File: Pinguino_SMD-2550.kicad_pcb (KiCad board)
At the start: 2 copper layers, 25.4 x 25.4 mm, 17 parts, among them P1 USB_OTG, P2 CONN_01X08, P3 CONN_01X02, P4 CONN_01X10, SW1 SW Reset, Y1 20Mhz

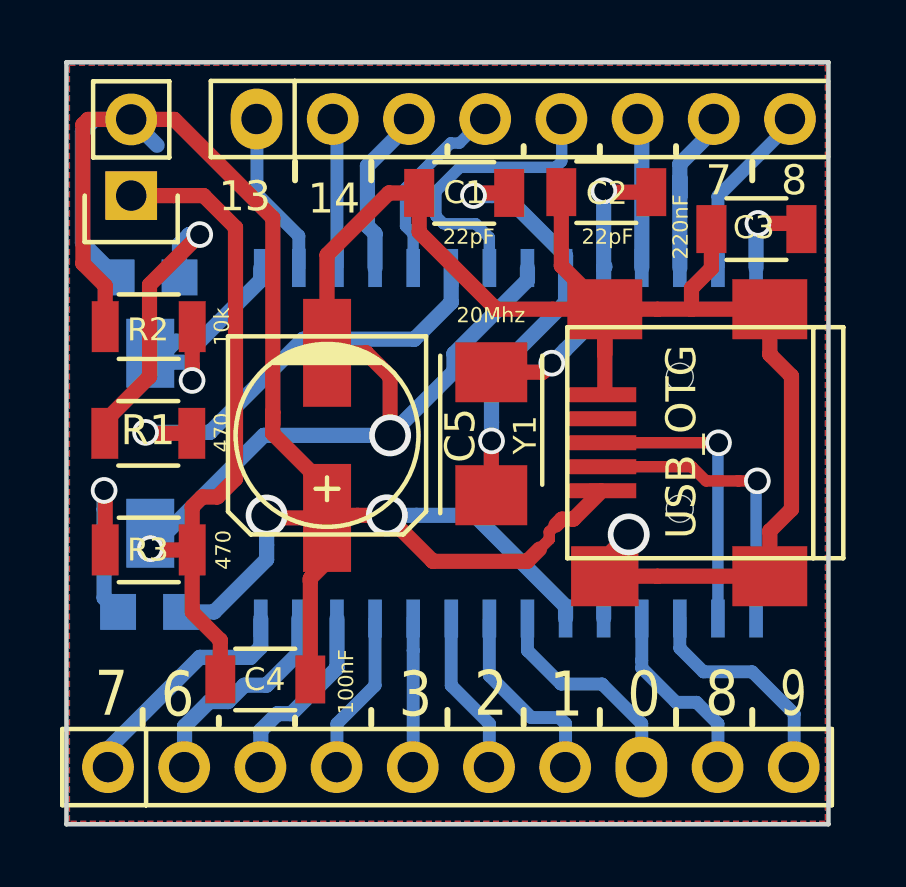
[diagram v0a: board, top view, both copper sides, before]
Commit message: Modify README.md file, updated BOM and add OSHW logo in SS layer.
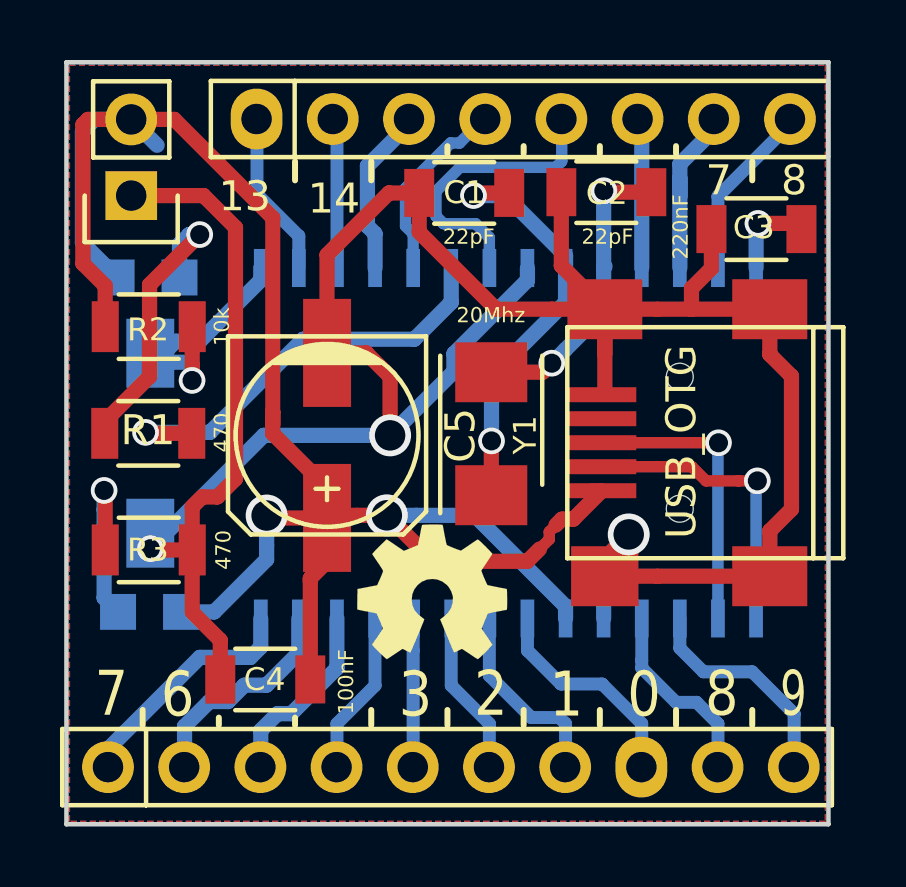
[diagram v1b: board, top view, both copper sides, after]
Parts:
- added G***: LOGO, LOGO, F.Cu at (42.7, 38.5)
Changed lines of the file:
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@@
 (kicad_pcb (version 4) (host pcbnew 4.0.2+dfsg1-2~bpo8+1-stable)
   (general
-    (links 0)
+    (links 51)
     (no_connects 0)
     (area 30.404999 20.752999 55.955001 46.303001)
@@
     (tracks 278)
     (zones 0)
-    (modules 17)
+    (modules 18)
     (nets 30)
   )
@@
   )
   (setup
-    (last_trace_width 0.508)
+    (last_trace_width 0.1524)
     (user_trace_width 0.1524)
     (user_trace_width 0.254)
@@
     (uvia_drill 0.254)
   )
+  (module LOGO (layer F.Cu)
+    (at 42.672 38.481)
+    (fp_text reference G*** (at 0 2.65176) (layer F.SilkS) hide
+      (effects (font (size 0.22606 0.22606) (thickness 0.04318)))
+    )
+    (fp_text value LOGO (at 0 -2.65176) (layer F.SilkS) hide
+      (effects (font (size 0.22606 0.22606) (thickness 0.04318)))
+    )
+    (fp_poly (pts (xy -1.51384 2.24536) (xy -1.48844 2.23012) (xy -1.43002 2.19456) (xy -1.3462 2.13868)
+      (xy -1.24714 2.07264) (xy -1.14808 2.0066) (xy -1.0668 1.95326) (xy -1.01092 1.91516)
+      (xy -0.98552 1.90246) (xy -0.97282 1.90754) (xy -0.9271 1.9304) (xy -0.85852 1.96596)
+      (xy -0.81788 1.98628) (xy -0.75692 2.01168) (xy -0.7239 2.0193) (xy -0.71882 2.00914)
+      (xy -0.69596 1.96088) (xy -0.6604 1.8796) (xy -0.61468 1.77038) (xy -0.5588 1.64338)
+      (xy -0.50292 1.50876) (xy -0.4445 1.36906) (xy -0.38862 1.23444) (xy -0.34036 1.11506)
+      (xy -0.29972 1.01854) (xy -0.27432 0.94996) (xy -0.26416 0.92202) (xy -0.2667 0.9144)
+      (xy -0.29972 0.88392) (xy -0.35306 0.84328) (xy -0.47244 0.74676) (xy -0.58928 0.60198)
+      (xy -0.6604 0.43688) (xy -0.68326 0.25146) (xy -0.66294 0.08128) (xy -0.5969 -0.08128)
+      (xy -0.4826 -0.2286) (xy -0.3429 -0.33782) (xy -0.18034 -0.4064) (xy 0 -0.42926)
+      (xy 0.17272 -0.40894) (xy 0.34036 -0.3429) (xy 0.48768 -0.23114) (xy 0.55118 -0.16002)
+      (xy 0.63754 -0.01016) (xy 0.6858 0.14732) (xy 0.69088 0.18796) (xy 0.68326 0.36322)
+      (xy 0.63246 0.5334) (xy 0.53848 0.68326) (xy 0.40894 0.80772) (xy 0.3937 0.81788)
+      (xy 0.33528 0.8636) (xy 0.29464 0.89408) (xy 0.26416 0.91948) (xy 0.48768 1.45796)
+      (xy 0.52324 1.54178) (xy 0.5842 1.6891) (xy 0.63754 1.8161) (xy 0.68072 1.9177)
+      (xy 0.7112 1.98374) (xy 0.7239 2.01168) (xy 0.7239 2.01422) (xy 0.74422 2.01676)
+      (xy 0.78486 2.00152) (xy 0.86106 1.96596) (xy 0.90932 1.94056) (xy 0.96774 1.91262)
+      (xy 0.99314 1.90246) (xy 1.016 1.91516) (xy 1.06934 1.95072) (xy 1.15062 2.00406)
+      (xy 1.24714 2.06756) (xy 1.33858 2.13106) (xy 1.4224 2.18694) (xy 1.48336 2.22504)
+      (xy 1.51384 2.24282) (xy 1.51892 2.24282) (xy 1.54432 2.22758) (xy 1.59258 2.18694)
+      (xy 1.66624 2.11836) (xy 1.77038 2.01422) (xy 1.78562 1.99898) (xy 1.87198 1.91262)
+      (xy 1.94056 1.83896) (xy 1.98628 1.78816) (xy 2.00406 1.7653) (xy 2.00406 1.7653)
+      (xy 1.98882 1.73482) (xy 1.95072 1.67386) (xy 1.89484 1.5875) (xy 1.82626 1.48844)
+      (xy 1.64846 1.22936) (xy 1.74498 0.98552) (xy 1.77546 0.90932) (xy 1.81356 0.82042)
+      (xy 1.8415 0.75438) (xy 1.85674 0.72644) (xy 1.88214 0.71628) (xy 1.95072 0.70104)
+      (xy 2.04724 0.68072) (xy 2.16154 0.6604) (xy 2.2733 0.64008) (xy 2.37236 0.61976)
+      (xy 2.44348 0.60706) (xy 2.4765 0.59944) (xy 2.48412 0.59436) (xy 2.49174 0.57912)
+      (xy 2.49428 0.5461) (xy 2.49682 0.48514) (xy 2.49936 0.39116) (xy 2.49936 0.25146)
+      (xy 2.49936 0.23622) (xy 2.49682 0.10668) (xy 2.49428 0) (xy 2.49174 -0.06604)
+      (xy 2.48666 -0.09398) (xy 2.48666 -0.09398) (xy 2.45618 -0.1016) (xy 2.38506 -0.11684)
+      (xy 2.286 -0.13462) (xy 2.16662 -0.15748) (xy 2.159 -0.16002) (xy 2.04216 -0.18288)
+      (xy 1.9431 -0.2032) (xy 1.87198 -0.21844) (xy 1.84404 -0.2286) (xy 1.83642 -0.23622)
+      (xy 1.81356 -0.28194) (xy 1.78054 -0.3556) (xy 1.7399 -0.4445) (xy 1.7018 -0.53848)
+      (xy 1.66878 -0.6223) (xy 1.64592 -0.68326) (xy 1.6383 -0.7112) (xy 1.64084 -0.71374)
+      (xy 1.65862 -0.74168) (xy 1.69926 -0.80264) (xy 1.75514 -0.88646) (xy 1.82372 -0.98806)
+      (xy 1.8288 -0.99568) (xy 1.89738 -1.09474) (xy 1.95326 -1.1811) (xy 1.98882 -1.23952)
+      (xy 2.00406 -1.26746) (xy 2.00406 -1.27) (xy 1.9812 -1.30048) (xy 1.9304 -1.35636)
+      (xy 1.85674 -1.43256) (xy 1.77038 -1.52146) (xy 1.74244 -1.54686) (xy 1.64338 -1.64338)
+      (xy 1.57734 -1.70434) (xy 1.53416 -1.73736) (xy 1.51384 -1.74498) (xy 1.51384 -1.74498)
+      (xy 1.48336 -1.7272) (xy 1.41986 -1.68656) (xy 1.33604 -1.62814) (xy 1.23444 -1.55956)
+      (xy 1.22682 -1.55448) (xy 1.12776 -1.4859) (xy 1.04394 -1.43002) (xy 0.98552 -1.38938)
+      (xy 0.95758 -1.37414) (xy 0.95504 -1.37414) (xy 0.9144 -1.38684) (xy 0.84328 -1.41224)
+      (xy 0.75438 -1.44526) (xy 0.66294 -1.48336) (xy 0.57912 -1.51892) (xy 0.51562 -1.54686)
+      (xy 0.48514 -1.56464) (xy 0.48514 -1.56464) (xy 0.47498 -1.6002) (xy 0.4572 -1.6764)
+      (xy 0.43688 -1.778) (xy 0.41148 -1.89992) (xy 0.40894 -1.92024) (xy 0.38608 -2.03962)
+      (xy 0.3683 -2.13868) (xy 0.35306 -2.20726) (xy 0.34544 -2.2352) (xy 0.3302 -2.23774)
+      (xy 0.27178 -2.24282) (xy 0.18288 -2.24536) (xy 0.07366 -2.24536) (xy -0.0381 -2.24536)
+      (xy -0.14732 -2.24282) (xy -0.2413 -2.24028) (xy -0.30988 -2.2352) (xy -0.33782 -2.23012)
+      (xy -0.33782 -2.22758) (xy -0.34798 -2.18948) (xy -0.36576 -2.11582) (xy -0.38608 -2.01168)
+      (xy -0.40894 -1.88976) (xy -0.41402 -1.8669) (xy -0.43688 -1.75006) (xy -0.4572 -1.651)
+      (xy -0.4699 -1.58496) (xy -0.47752 -1.55702) (xy -0.49022 -1.55194) (xy -0.53848 -1.53162)
+      (xy -0.61722 -1.4986) (xy -0.71628 -1.45796) (xy -0.94488 -1.36652) (xy -1.22682 -1.55702)
+      (xy -1.25222 -1.5748) (xy -1.35382 -1.64338) (xy -1.4351 -1.69926) (xy -1.49352 -1.73736)
+      (xy -1.51638 -1.75006) (xy -1.51892 -1.75006) (xy -1.54686 -1.72466) (xy -1.60274 -1.67132)
+      (xy -1.67894 -1.59766) (xy -1.76784 -1.5113) (xy -1.83134 -1.44526) (xy -1.91008 -1.36652)
+      (xy -1.95834 -1.31318) (xy -1.98628 -1.28016) (xy -1.9939 -1.25984) (xy -1.99136 -1.2446)
+      (xy -1.97358 -1.21666) (xy -1.93294 -1.1557) (xy -1.87452 -1.06934) (xy -1.80594 -0.97028)
+      (xy -1.75006 -0.88646) (xy -1.6891 -0.79248) (xy -1.651 -0.72644) (xy -1.63576 -0.69342)
+      (xy -1.64084 -0.68072) (xy -1.65862 -0.62484) (xy -1.69418 -0.54102) (xy -1.73482 -0.44196)
+      (xy -1.83388 -0.22098) (xy -1.97866 -0.19304) (xy -2.06756 -0.17526) (xy -2.18948 -0.1524)
+      (xy -2.30886 -0.12954) (xy -2.49174 -0.09398) (xy -2.49936 0.58166) (xy -2.47142 0.59436)
+      (xy -2.44348 0.60198) (xy -2.3749 0.61722) (xy -2.27838 0.63754) (xy -2.16154 0.65786)
+      (xy -2.06502 0.67564) (xy -1.96596 0.69596) (xy -1.89484 0.70866) (xy -1.86436 0.71628)
+      (xy -1.8542 0.72644) (xy -1.83134 0.7747) (xy -1.79578 0.8509) (xy -1.75514 0.94234)
+      (xy -1.71704 1.03632) (xy -1.68148 1.12522) (xy -1.65862 1.19126) (xy -1.64846 1.22428)
+      (xy -1.66116 1.25222) (xy -1.69926 1.31064) (xy -1.7526 1.39192) (xy -1.82118 1.49098)
+      (xy -1.88722 1.5875) (xy -1.94564 1.67132) (xy -1.98374 1.73228) (xy -2.00152 1.76022)
+      (xy -1.99136 1.778) (xy -1.95326 1.82626) (xy -1.8796 1.90246) (xy -1.76784 2.01168)
+      (xy -1.75006 2.02946) (xy -1.6637 2.11328) (xy -1.59004 2.18186) (xy -1.5367 2.22758)
+      (xy -1.51384 2.24536)) (layer F.SilkS) (width 0.00254))
+  )
   (module Buttons_Switches_SMD:SW_SMD_1181 (layer B.Cu)
